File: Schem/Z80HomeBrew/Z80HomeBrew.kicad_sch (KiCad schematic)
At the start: 0 parts

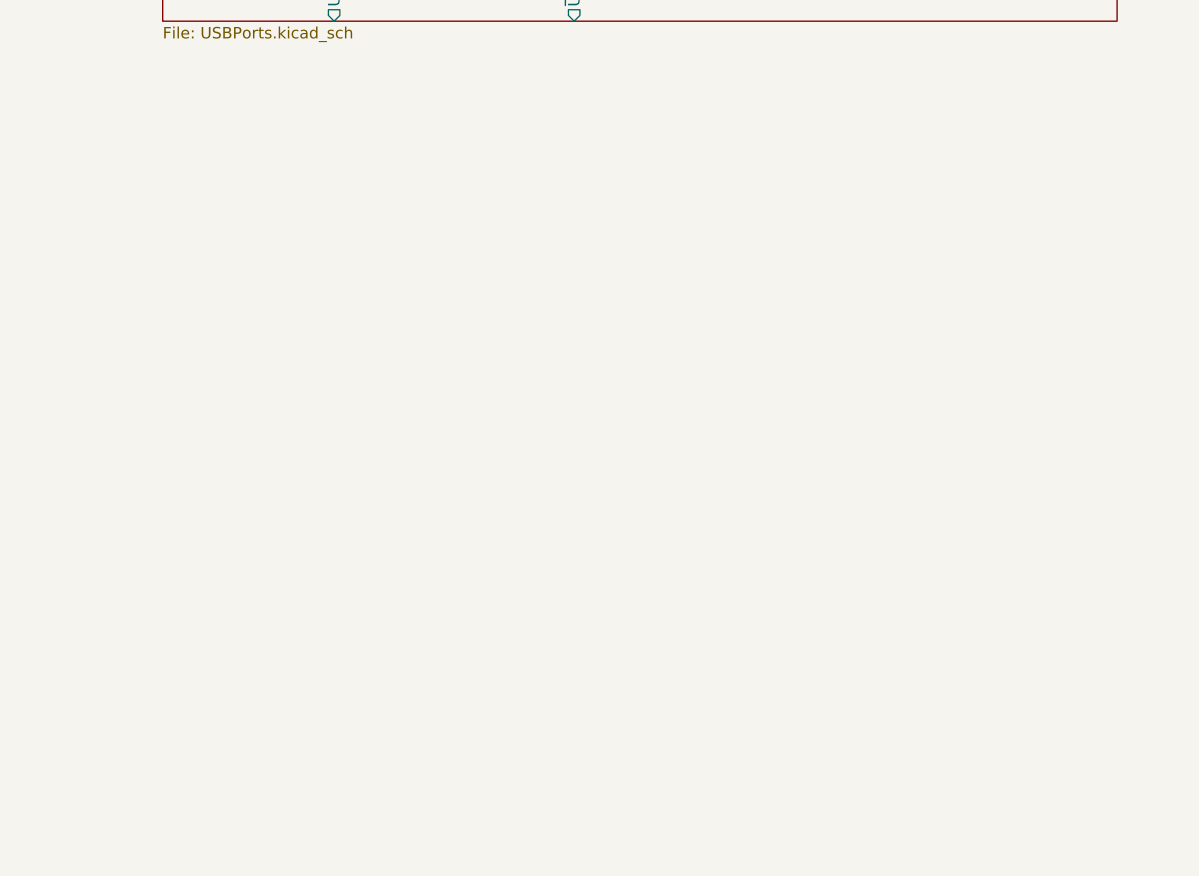
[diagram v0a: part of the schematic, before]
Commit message: Added sound, fixed safe space in memory map, updated CPU address decoding schematic.
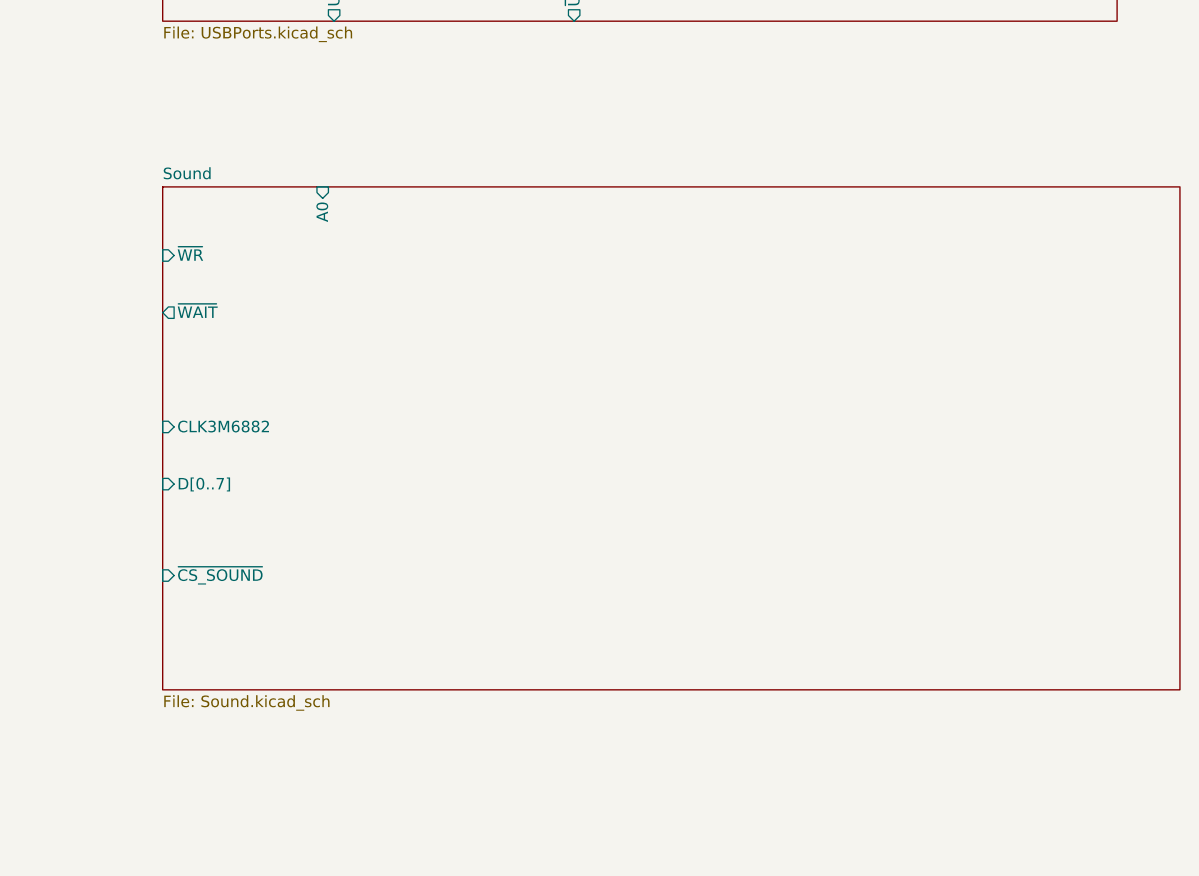
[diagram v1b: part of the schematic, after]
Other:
- added sheet Sound (Sound.kicad_sch)
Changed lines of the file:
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@@
+	)
+	(sheet
+		(at 294.64 102.87)
+		(size 113.03 55.88)
+		(exclude_from_sim no)
+		(in_bom yes)
+		(on_board yes)
+		(dnp no)
+		(fields_autoplaced yes)
+		(stroke
+			(width 0.1524)
+			(type solid)
+		)
+		(fill
+			(color 0 0 0 0.0000)
+		)
+		(property "Sheetname" "Sound"
+			(at 294.64 102.1584 0)
+			(effects
+				(font
+					(size 1.27 1.27)
+				)
+				(justify left bottom)
+			)
+		)
+		(property "Sheetfile" "Sound.kicad_sch"
+			(at 294.64 159.3346 0)
+			(effects
+				(font
+					(size 1.27 1.27)
+				)
+				(justify left top)
+			)
+		)
+		(pin "CLK3M6882" input
+			(at 294.64 129.54 180)
+			(effects
+				(font
+					(size 1.27 1.27)
+				)
+				(justify left)
+			)
+		)
+		(pin "D[0..7]" input
+			(at 294.64 135.89 180)
+			(effects
+				(font
+					(size 1.27 1.27)
+				)
+				(justify left)
+			)
+		)
+		(pin "~{CS_SOUND}" input
+			(at 294.64 146.05 180)
+			(effects
+				(font
+					(size 1.27 1.27)
+				)
+				(justify left)
+			)
+		)
+		(pin "~{WAIT}" output
+			(at 294.64 116.84 180)
+			(effects
+				(font
+					(size 1.27 1.27)
+				)
+				(justify left)
+			)
+		)
+		(pin "~{WR}" input
+			(at 294.64 110.49 180)
+			(effects
+				(font
+					(size 1.27 1.27)
+				)
+				(justify left)
+			)
+		)
+		(pin "A0" input
+			(at 312.42 102.87 90)
+			(effects
+				(font
+					(size 1.27 1.27)
+				)
+				(justify right)
+			)
+		)
+		(instances
+			(project "Z80HomeBrew"
+				(path "/5593e793-d133-45d0-a91e-72805049e474"
+					(page "9")
+				)
+			)
+		)
 	)
 	(sheet
